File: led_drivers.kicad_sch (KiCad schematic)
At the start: 6 parts, among them IC1 SamacSys_Parts_HT16K33-28SOP, IC2 SamacSys_Parts_HT16K33-28SOP

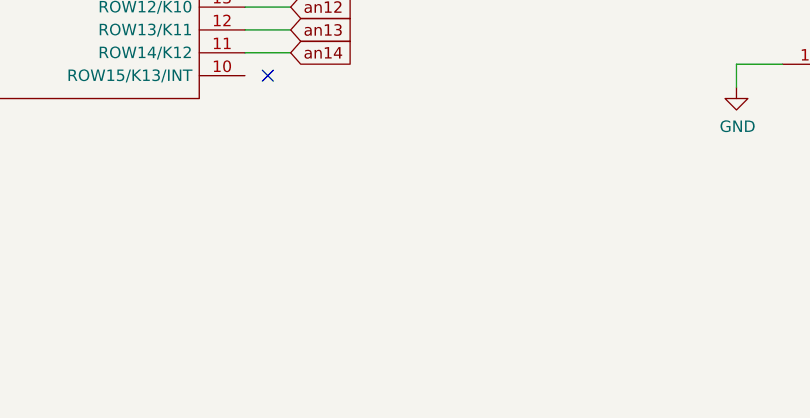
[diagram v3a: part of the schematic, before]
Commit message: Add 6mm omron tactile switches
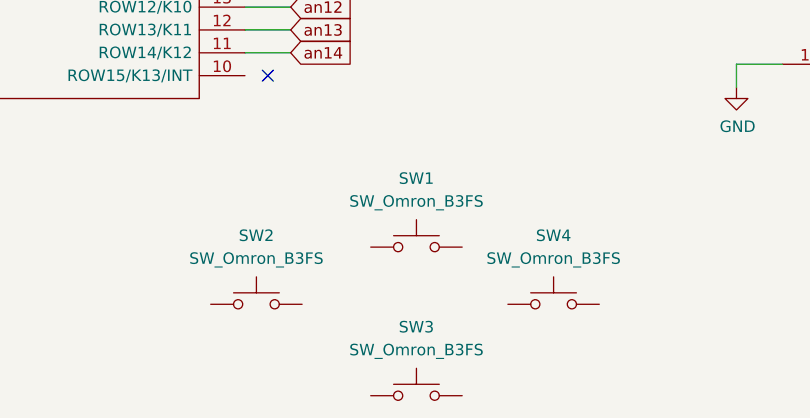
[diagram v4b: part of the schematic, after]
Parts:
- added SW1, SW2, SW3, SW4: SW_Omron_B3FS, Button_Switch_THT:SW_PUSH_6mm_H4.3mm, symbol Switch:SW_Omron_B3FS
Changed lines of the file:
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@@
+    )
+  )
+  (symbol (lib_id "Switch:SW_Omron_B3FS") (at 111.76 149.86 0) (unit 1)
+    (in_bom yes) (on_board yes) (dnp no) (fields_autoplaced)
+    (property "Reference" "SW3" (at 111.76 142.24 0)
+      (effects (font (size 1.27 1.27)))
+    )
+    (property "Value" "SW_Omron_B3FS" (at 111.76 144.78 0)
+      (effects (font (size 1.27 1.27)))
+    )
+    (property "Footprint" "Button_Switch_THT:SW_PUSH_6mm_H4.3mm" (at 111.76 144.78 0)
+      (effects (font (size 1.27 1.27)) hide)
+    )
+    (property "Datasheet" "https://omronfs.omron.com/en_US/ecb/products/pdf/en-b3fs.pdf" (at 111.76 144.78 0)
+      (effects (font (size 1.27 1.27)) hide)
+    )
+    (pin "1")
+    (pin "2")
+    (instances
+      (project "ltp_kikad"
+        (path "/eed35b77-cbf9-4596-9b17-2558f81058ba/7d22e16e-a0ba-4766-b1de-c8cbb28f14f7"
+          (reference "SW3") (unit 1)
+        )
+      )
+    )
+  )
+  (symbol (lib_id "Switch:SW_Omron_B3FS") (at 111.76 133.35 0) (unit 1)
+    (in_bom yes) (on_board yes) (dnp no) (fields_autoplaced)
+    (property "Reference" "SW1" (at 111.76 125.73 0)
+      (effects (font (size 1.27 1.27)))
+    )
+    (property "Value" "SW_Omron_B3FS" (at 111.76 128.27 0)
+      (effects (font (size 1.27 1.27)))
+    )
+    (property "Footprint" "Button_Switch_THT:SW_PUSH_6mm_H4.3mm" (at 111.76 128.27 0)
+      (effects (font (size 1.27 1.27)) hide)
+    )
+    (property "Datasheet" "https://omronfs.omron.com/en_US/ecb/products/pdf/en-b3fs.pdf" (at 111.76 128.27 0)
+      (effects (font (size 1.27 1.27)) hide)
+    )
+    (pin "1")
+    (pin "2")
+    (instances
+      (project "ltp_kikad"
+        (path "/eed35b77-cbf9-4596-9b17-2558f81058ba/7d22e16e-a0ba-4766-b1de-c8cbb28f14f7"
+          (reference "SW1") (unit 1)
+        )
+      )
     )
   )
@@
         (path "/eed35b77-cbf9-4596-9b17-2558f81058ba/7d22e16e-a0ba-4766-b1de-c8cbb28f14f7"
           (reference "C1") (unit 1)
+        )
+      )
+    )
+  )
+  (symbol (lib_id "Switch:SW_Omron_B3FS") (at 127 139.7 0) (unit 1)
+    (in_bom yes) (on_board yes) (dnp no) (fields_autoplaced)
+    (property "Reference" "SW4" (at 127 132.08 0)
+      (effects (font (size 1.27 1.27)))
+    )
+    (property "Value" "SW_Omron_B3FS" (at 127 134.62 0)
+      (effects (font (size 1.27 1.27)))
+    )
+    (property "Footprint" "Button_Switch_THT:SW_PUSH_6mm_H4.3mm" (at 127 134.62 0)
+      (effects (font (size 1.27 1.27)) hide)
+    )
+    (property "Datasheet" "https://omronfs.omron.com/en_US/ecb/products/pdf/en-b3fs.pdf" (at 127 134.62 0)
+      (effects (font (size 1.27 1.27)) hide)
+    )
+    (pin "1")
+    (pin "2")
+    (instances
+      (project "ltp_kikad"
+        (path "/eed35b77-cbf9-4596-9b17-2558f81058ba/7d22e16e-a0ba-4766-b1de-c8cbb28f14f7"
+          (reference "SW4") (unit 1)
         )
       )
@@
         )
       )
+    )
+  )
+  (symbol (lib_id "Switch:SW_Omron_B3FS") (at 93.98 139.7 0) (unit 1)
+    (in_bom yes) (on_board yes) (dnp no) (fields_autoplaced)
+    (property "Reference" "SW2" (at 93.98 132.08 0)
+      (effects (font (size 1.27 1.27)))
+    )
+    (property "Value" "SW_Omron_B3FS" (at 93.98 134.62 0)
+      (effects (font (size 1.27 1.27)))
+    )
+    (property "Footprint" "Button_Switch_THT:SW_PUSH_6mm_H4.3mm" (at 93.98 134.62 0)
+      (effects (font (size 1.27 1.27)) hide)
+    )
+    (property "Datasheet" "https://omronfs.omron.com/en_US/ecb/products/pdf/en-b3fs.pdf" (at 93.98 134.62 0)
+      (effects (font (size 1.27 1.27)) hide)
+    )
+    (pin "1")
+    (pin "2")
+    (instances
+      (project "ltp_kikad"
+        (path "/eed35b77-cbf9-4596-9b17-2558f81058ba/7d22e16e-a0ba-4766-b1de-c8cbb28f14f7"
+          (reference "SW2") (unit 1)
+        )
+      )

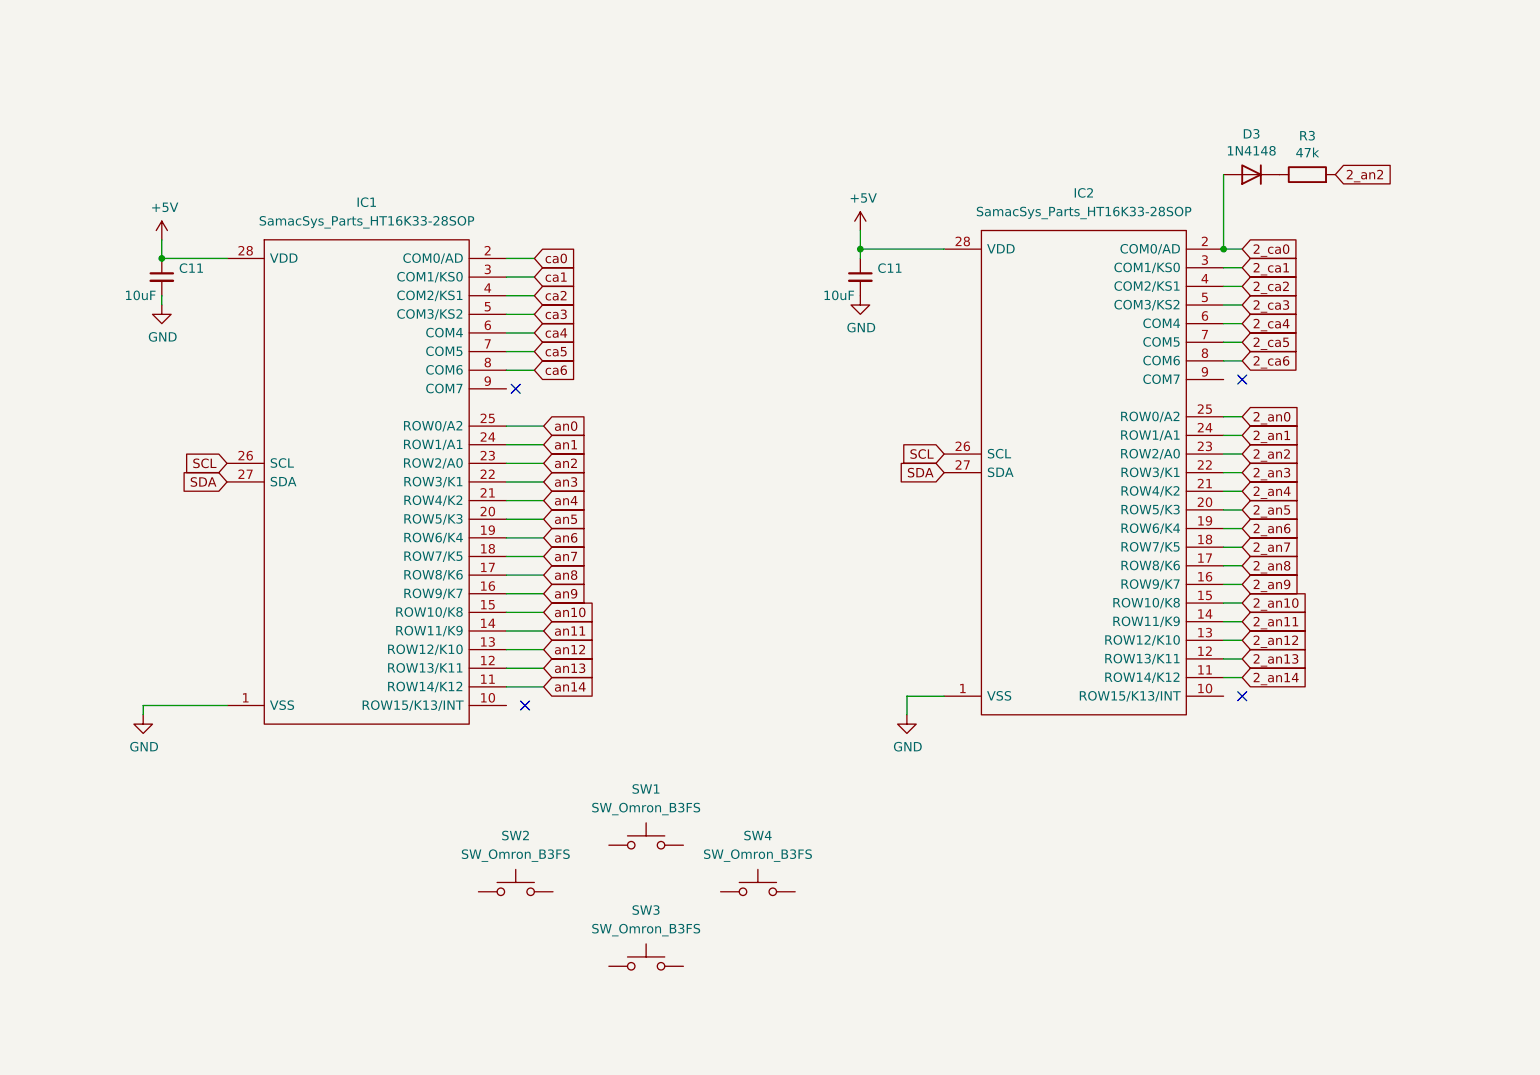
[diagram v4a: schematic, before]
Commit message: Route switches connections
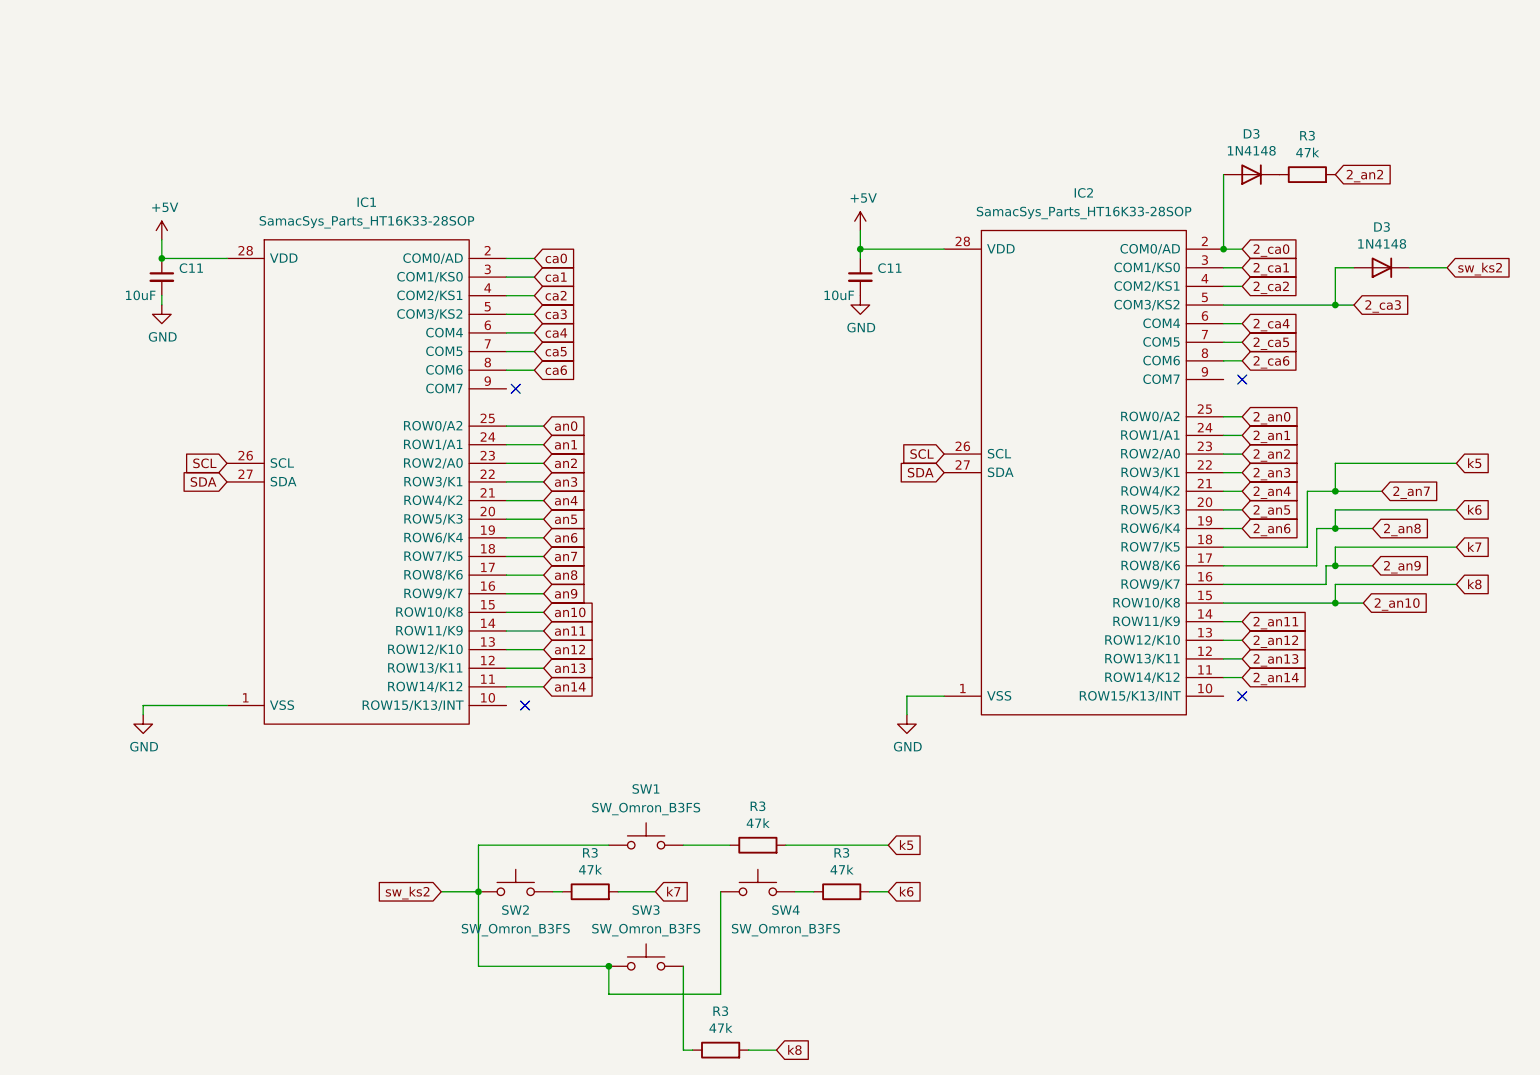
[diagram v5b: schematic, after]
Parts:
- added D3: 1N4148, Diode_SMD:D_0805_2012Metric, symbol Device:D
- added R3 (x4): 47k, Resistor_SMD:R_0603_1608Metric, symbol Device:R
- D3: footprint Diode_SMD:D_SOD-123 -> Diode_SMD:D_0805_2012Metric
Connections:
- net 2_an10: now also R3.2
- net 2_an7: now also R3.2
- net 2_an8: now also R3.2
- net 2_an9: now also R3.2
- net 2_ca3: now also D3.2 (A)
- net sw_ks2: now reaches SW3.1
- net sw_ks2: now also SW1.1, SW2.1, SW4.1, D3.1 (K)
- net at SW3.2: now also R3.1
- net at SW1.2: now also R3.1
- net at SW4.2: now also R3.1
- net at SW2.2: now also R3.1

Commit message: Pitanga Hat V1
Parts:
- added C11: 10uF, Capacitor_SMD:C_0603_1608Metric, symbol Device:C_Small
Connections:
- net +5V: now also C11.1
- net GND: now also C11.2
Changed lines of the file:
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@@
+    (stroke (width 0) (type default))
+  )
+  (wire (pts (xy 133.35 49.53) (xy 133.35 53.34))
     (stroke (width 0) (type default))
   )
@@
     )
   )
+  (symbol (lib_id "Device:C_Small") (at 133.35 55.88 0) (unit 1)
+    (in_bom yes) (on_board yes) (dnp no)
+    (property "Reference" "C11" (at 135.6868 54.7116 0)
+      (effects (font (size 1.27 1.27)) (justify left))
+    )
+    (property "Value" "10uF" (at 128.27 58.42 0)
+      (effects (font (size 1.27 1.27)) (justify left))
+    )
+    (property "Footprint" "Capacitor_SMD:C_0603_1608Metric" (at 133.35 55.88 0)
+      (effects (font (size 1.27 1.27)) hide)
+    )
+    (property "Datasheet" "~" (at 133.35 55.88 0)
+      (effects (font (size 1.27 1.27)) hide)
+    )
+    (pin "1")
+    (pin "2")
+    (instances
+      (project "LTP305_ESP32_CLOCK"
+        (path "/c007e288-8439-49d9-bbdf-49724c34958c"
+          (reference "C11") (unit 1)
+        )
+      )
+      (project "ltp_kikad"
+        (path "/eed35b77-cbf9-4596-9b17-2558f81058ba"
+          (reference "C2") (unit 1)
+        )
+        (path "/eed35b77-cbf9-4596-9b17-2558f81058ba/7d22e16e-a0ba-4766-b1de-c8cbb28f14f7"
+          (reference "C4") (unit 1)
+        )
+      )
+    )
+  )
   (symbol (lib_id "Device:D") (at 212.09 54.61 180) (unit 1)
     (in_bom yes) (on_board yes) (dnp no)
@@
         )
       )
+    )
+  )
+  (symbol (lib_id "power:+5V") (at 133.35 49.53 0) (unit 1)
+    (in_bom yes) (on_board yes) (dnp no)
+    (property "Reference" "#PWR08" (at 133.35 53.34 0)
+      (effects (font (size 1.27 1.27)) hide)
+    )
+    (property "Value" "+5V" (at 133.731 45.1358 0)
+      (effects (font (size 1.27 1.27)))
+    )
+    (property "Footprint" "" (at 133.35 49.53 0)
+      (effects (font (size 1.27 1.27)) hide)
+    )
+    (property "Datasheet" "" (at 133.35 49.53 0)
+      (effects (font (size 1.27 1.27)) hide)
+    )
+    (pin "1")
+    (instances
+      (project "LTP305_ESP32_CLOCK"
+        (path "/c007e288-8439-49d9-bbdf-49724c34958c"
+          (reference "#PWR08") (unit 1)
+        )
+      )
+      (project "ltp_kikad"
+        (path "/eed35b77-cbf9-4596-9b17-2558f81058ba"
+          (reference "#PWR04") (unit 1)
+        )
+        (path "/eed35b77-cbf9-4596-9b17-2558f81058ba/7d22e16e-a0ba-4766-b1de-c8cbb28f14f7"
+          (reference "#PWR020") (unit 1)
+        )
+      )
+    )
+  )
+  (symbol (lib_id "power:GND") (at 133.35 58.42 0) (unit 1)
+    (in_bom yes) (on_board yes) (dnp no)
+    (property "Reference" "#PWR038" (at 133.35 64.77 0)
+      (effects (font (size 1.27 1.27)) hide)
+    )
+    (property "Value" "GND" (at 133.477 62.8142 0)
+      (effects (font (size 1.27 1.27)))
+    )
+    (property "Footprint" "" (at 133.35 58.42 0)
+      (effects (font (size 1.27 1.27)) hide)
+    )
+    (property "Datasheet" "" (at 133.35 58.42 0)
+      (effects (font (size 1.27 1.27)) hide)
+    )
+    (pin "1")
+    (instances
+      (project "LTP305_ESP32_CLOCK"
+        (path "/c007e288-8439-49d9-bbdf-49724c34958c"
+          (reference "#PWR038") (unit 1)
+        )
+      )
+      (project "ltp_kikad"
+        (path "/eed35b77-cbf9-4596-9b17-2558f81058ba"
+          (reference "#PWR05") (unit 1)
+        )
+        (path "/eed35b77-cbf9-4596-9b17-2558f81058ba/7d22e16e-a0ba-4766-b1de-c8cbb28f14f7"
+          (reference "#PWR021") (unit 1)
+        )
+      )

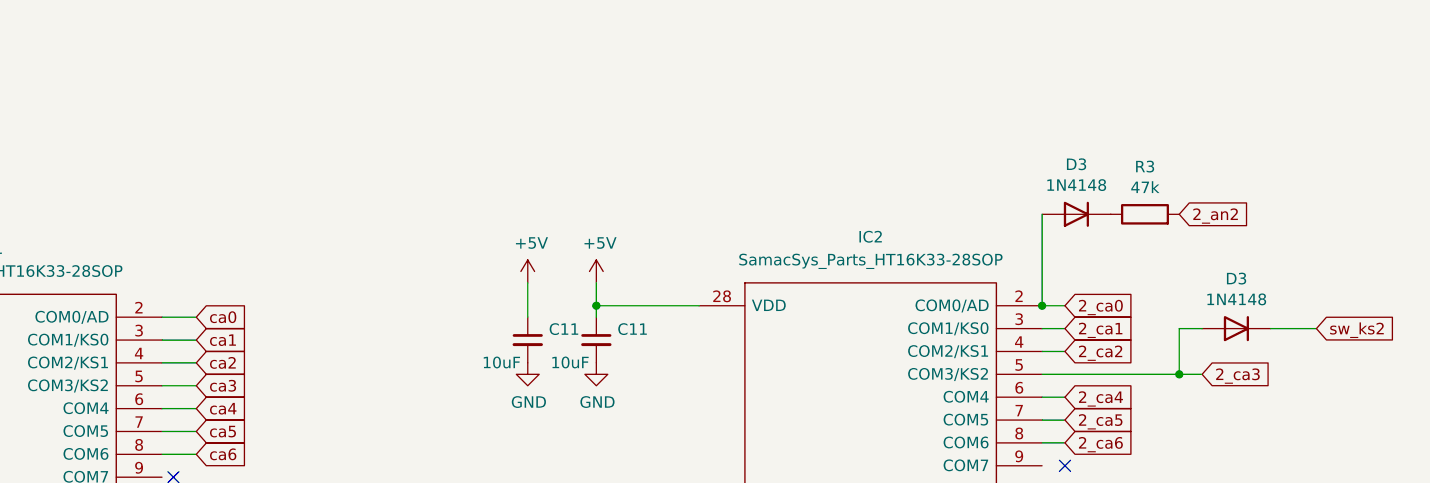
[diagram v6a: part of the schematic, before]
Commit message: Add address resistors
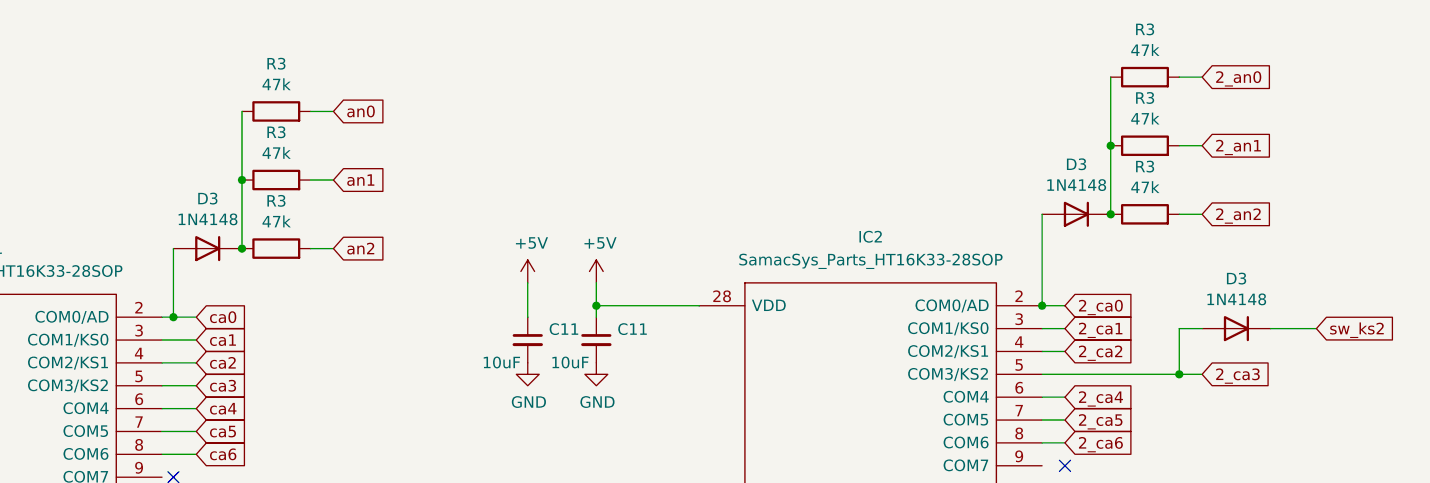
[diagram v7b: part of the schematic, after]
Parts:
- added D3: 1N4148, Diode_SMD:D_0805_2012Metric, symbol Device:D
- added R3 (x5): 47k, Resistor_SMD:R_0603_1608Metric, symbol Device:R
- R3: Function (none) -> A0
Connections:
- net 2_an0: now also R3.2
- net 2_an1: now also R3.2
- net an0: now also R3.2
- net an1: now also R3.2
- net an2: now also R3.2
- net ca0: now also D3.2 (A)
- net at D3.1 (K), R3.1: now also R3.1, R3.1
- new net: D3.1 (K), R3.1, R3.1, R3.1
